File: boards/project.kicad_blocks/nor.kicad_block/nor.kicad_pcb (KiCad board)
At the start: 2 copper layers, 3 parts, among them Q2 MMBT5401

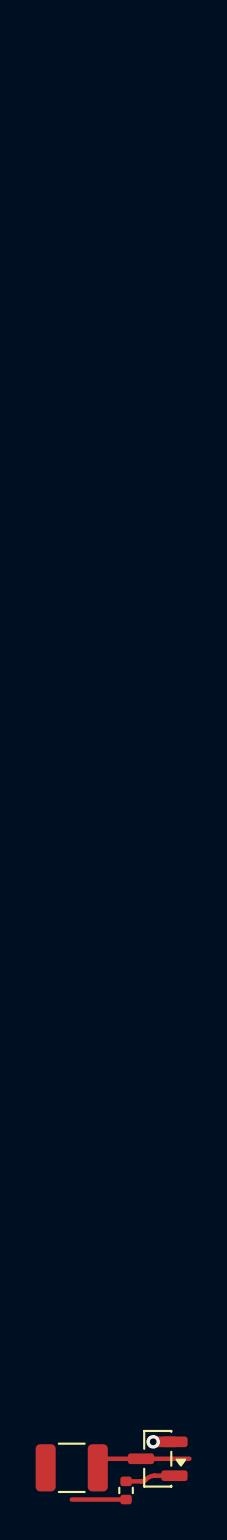
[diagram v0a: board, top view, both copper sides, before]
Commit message: Route left column passives.
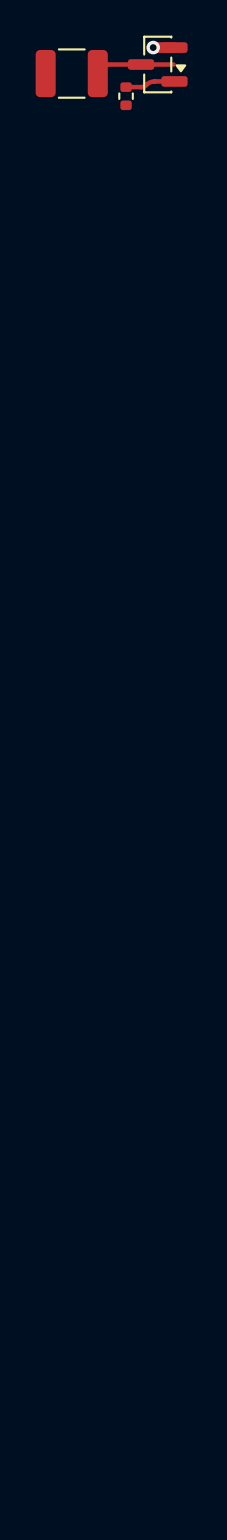
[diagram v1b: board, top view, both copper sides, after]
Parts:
- removed Q2: MMBT5401, Package_TO_SOT_SMD:SOT-23
- removed R3: 56k, Resistor_SMD:R_0402_1005Metric
- removed R4: 2k ½W, Resistor_SMD:R_1210_3225Metric
- added Q24: MMBT5401, Package_TO_SOT_SMD:SOT-23, F.Cu at (87.4, 77.5)
- added R41: 56k, Resistor_SMD:R_0402_1005Metric, F.Cu at (85.6, 79.2)
- added R42: 2k ½W, Resistor_SMD:R_1210_3225Metric, F.Cu at (82.5, 78.0)
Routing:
- net Net-(Q2-C): track 5.35 -> 0.00 mm
- net Net-(Q24-C): track 0.00 -> 4.46 mm
- net +15V: track 3.05 -> 0.00 mm
- net Net-(Q2-B): track 2.80 -> 0.00 mm
- net Net-(Q24-B): track 0.00 -> 2.80 mm

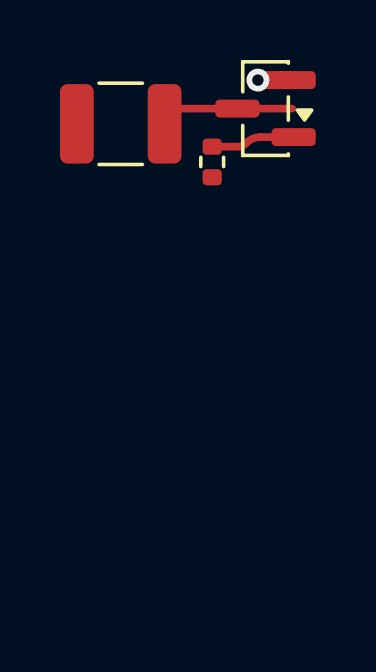
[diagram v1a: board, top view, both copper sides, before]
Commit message: More rough routing.
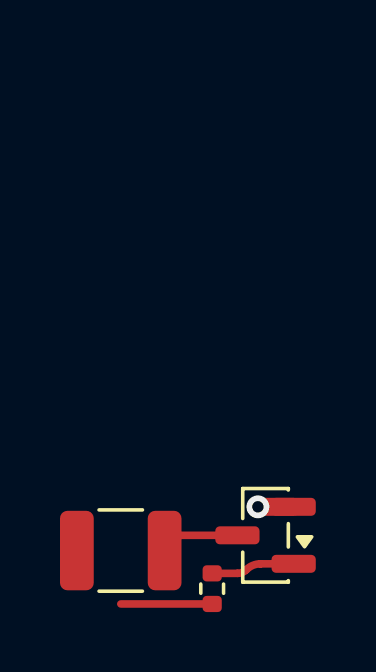
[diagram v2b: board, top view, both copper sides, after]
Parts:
- removed Q24: MMBT5401, Package_TO_SOT_SMD:SOT-23
- removed R41: 56k, Resistor_SMD:R_0402_1005Metric
- removed R42: 2k ½W, Resistor_SMD:R_1210_3225Metric
- added Q20: MMBT5401, Package_TO_SOT_SMD:SOT-23, F.Cu at (87.4, 91.7)
- added R35: 56k, Resistor_SMD:R_0402_1005Metric, F.Cu at (85.6, 93.5)
- added R36: 2k ½W, Resistor_SMD:R_1210_3225Metric, F.Cu at (82.5, 92.2)
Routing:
- net Net-(Q24-C): track 4.46 -> 0.00 mm
- net +15V: track 0.00 -> 3.05 mm
- net Net-(Q24-B): track 2.80 -> 0.00 mm
- net Net-(Q20-B): track 0.00 -> 2.80 mm
- net Net-(Q20-C): track 0.00 -> 2.64 mm
